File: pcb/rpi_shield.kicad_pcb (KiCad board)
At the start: 2 copper layers, 65 x 56 mm, 22 parts, among them IC1 ATTINY48-A, P1 CONN_02X20, P101 CONN_01X02, P102 CONN_01X02, P103 CONN_01X02, P104 CONN_01X02, Q1 AM4874N, Q2 AM4874N, Q3 AM4874N, U101 LM317AEMP

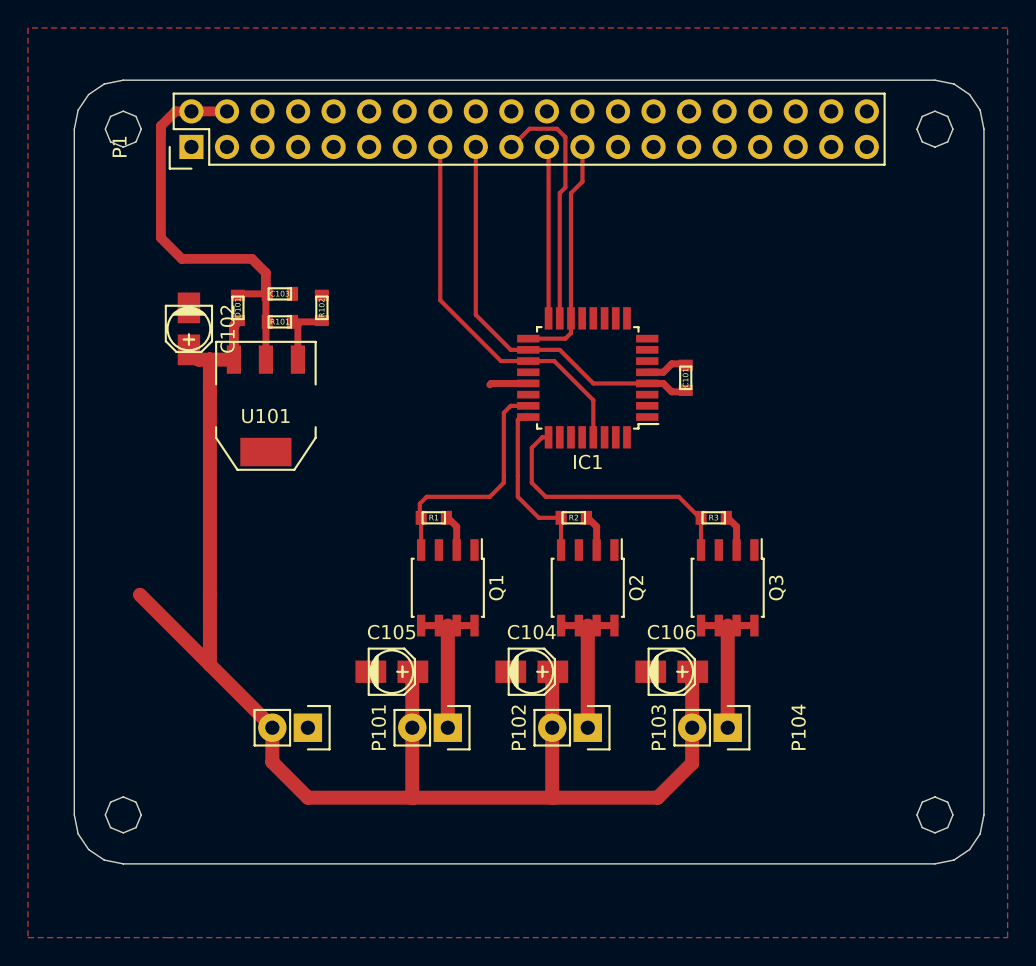
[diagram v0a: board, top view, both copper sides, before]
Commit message: swapped the mcu to a dac and a quad opamp
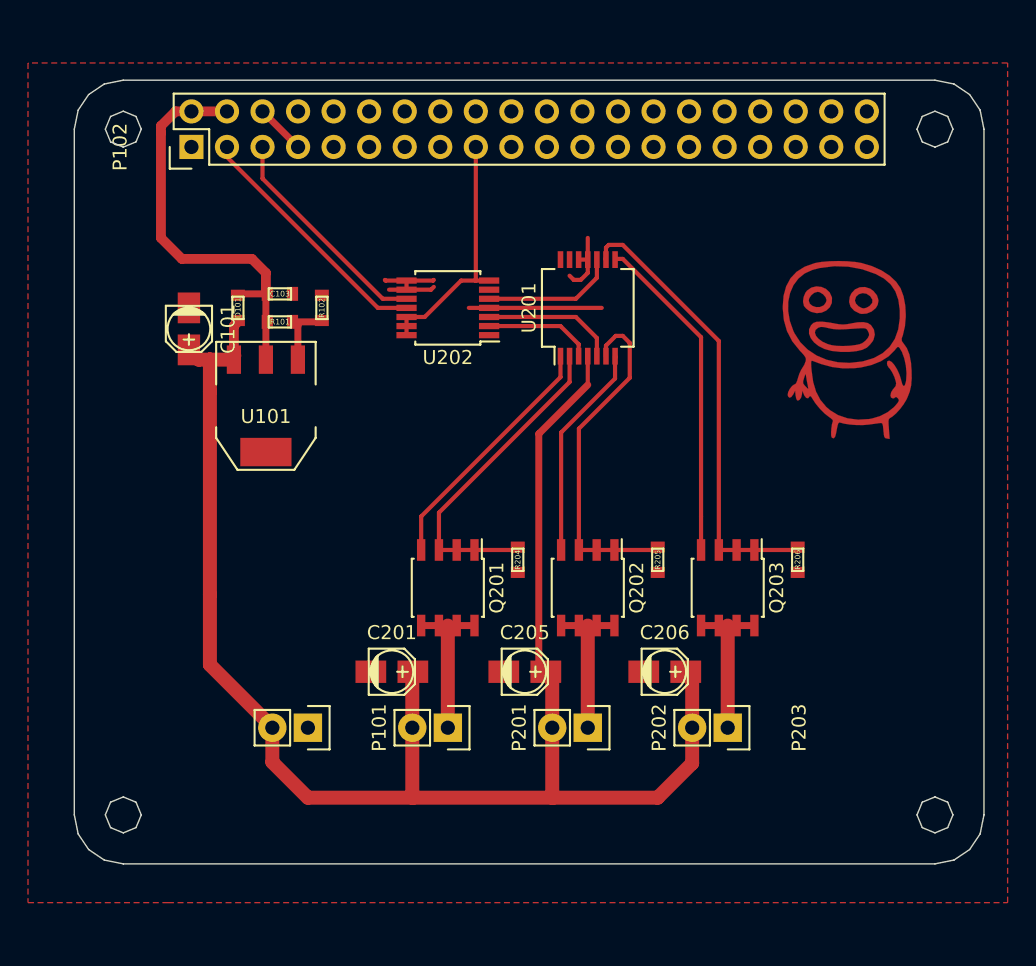
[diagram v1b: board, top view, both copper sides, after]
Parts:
- removed C102, C104, C105, C106: C, Capacitors_SMD:c_elec_3x5.3
- removed IC1: ATTINY48-A, Housings_QFP:TQFP-32_7x7mm_Pitch0.8mm
- removed P1: CONN_02X20, Pin_Headers:Pin_Header_Straight_2x20
- removed P103, P104: CONN_01X02, Pin_Headers:Pin_Header_Straight_1x02
- removed Q1, Q2, Q3: AM4874N, Housings_SOIC:SOIC-8_3.9x4.9mm_Pitch1.27mm
- removed R1, R2, R3: R, netl:SMD_0603
- added C201: C, Capacitors_SMD:c_elec_3x5.3, F.Cu at (121.0, 101.0)
- added C205: C, Capacitors_SMD:c_elec_3x5.3, F.Cu at (130.5, 101.0)
- added C206: C, Capacitors_SMD:c_elec_3x5.3, F.Cu at (140.5, 101.0)
- added G***: LOGO, netl:LOGO_127mm_copper, F.Cu at (153.5, 78.0)
- added P201: CONN_01X02, Pin_Headers:Pin_Header_Straight_1x02, F.Cu at (125.0, 105.0)
- added P202: CONN_01X02, Pin_Headers:Pin_Header_Straight_1x02, F.Cu at (135.0, 105.0)
- added P203: CONN_01X02, Pin_Headers:Pin_Header_Straight_1x02, F.Cu at (145.0, 105.0)
- added Q201: AM4874N, Housings_SOIC:SOIC-8_3.9x4.9mm_Pitch1.27mm, F.Cu at (125.0, 95.0)
- added Q202: AM4874N, Housings_SOIC:SOIC-8_3.9x4.9mm_Pitch1.27mm, F.Cu at (135.0, 95.0)
- added Q203: AM4874N, Housings_SOIC:SOIC-8_3.9x4.9mm_Pitch1.27mm, F.Cu at (145.0, 95.0)
- added R204: R, netl:SMD_0603, F.Cu at (130.0, 93.0)
- added R205: R, netl:SMD_0603, F.Cu at (140.0, 93.0)
- added R206: R, netl:SMD_0603, F.Cu at (150.0, 93.0)
- added U201: LM2902N, Housings_SSOP:SSOP-14_5.3x6.2mm_Pitch0.65mm, F.Cu at (135.0, 75.0)
- added U202: MAX5813, Housings_SSOP:TSSOP-14_4.4x5mm_Pitch0.65mm, F.Cu at (125.0, 75.0)
- C101: footprint netl:SMD_0603 -> Capacitors_SMD:c_elec_3x5.3
- P102: value CONN_01X02 -> CONN_02X20; footprint Pin_Headers:Pin_Header_Straight_1x02 -> Pin_Headers:Pin_Header_Straight_2x20
- moved P102 45.4 mm to (106.7, 63.5), turned to 90 degrees
- moved C101 35.7 mm to (106.5, 76.5), turned to 270 degrees
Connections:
- C101 pad 1: 3v3 -> Vdd
- P102 pad 1: /DrainRed -> 3v3
- P102 pad 2: Vdd -> 5V
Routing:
- net Net-(Q203-Pad1): track 0.00 -> 32.6 mm
- net RESET: track 27.5 -> 0.06 mm
- net Net-(Q202-Pad1): track 0.00 -> 25.0 mm
- net Net-(Q203-Pad4): track 0.00 -> 23.7 mm
- net Net-(Q201-Pad1): track 0.00 -> 23.6 mm
- net Net-(Q201-Pad4): track 0.00 -> 18.5 mm
- net SDA: track 0.00 -> 18.0 mm
- net Vdd: track 104.3 -> 122.1 mm
- net MOSI: track 17.8 -> 0.00 mm
- net SCK: track 16.9 -> 0.00 mm
- net SCL: track 0.00 -> 16.1 mm
- net Net-(Q202-Pad4): track 0.00 -> 15.5 mm
- net MISO: track 12.3 -> 0.34 mm
- net GND: track 13.5 -> 25.3 mm
- net /LED driver/DrainRed: track 0.00 -> 11.5 mm
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
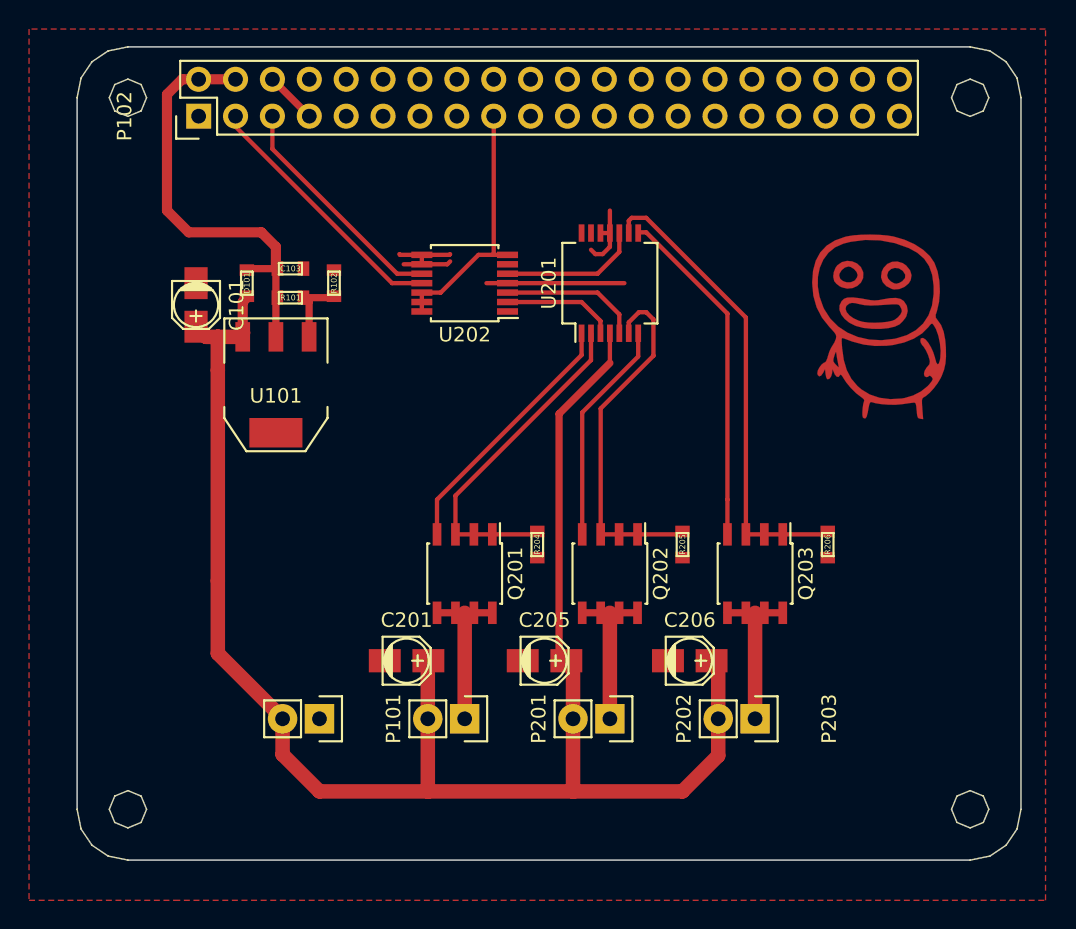
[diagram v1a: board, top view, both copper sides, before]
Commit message: removed excess power pins. moved parts around.
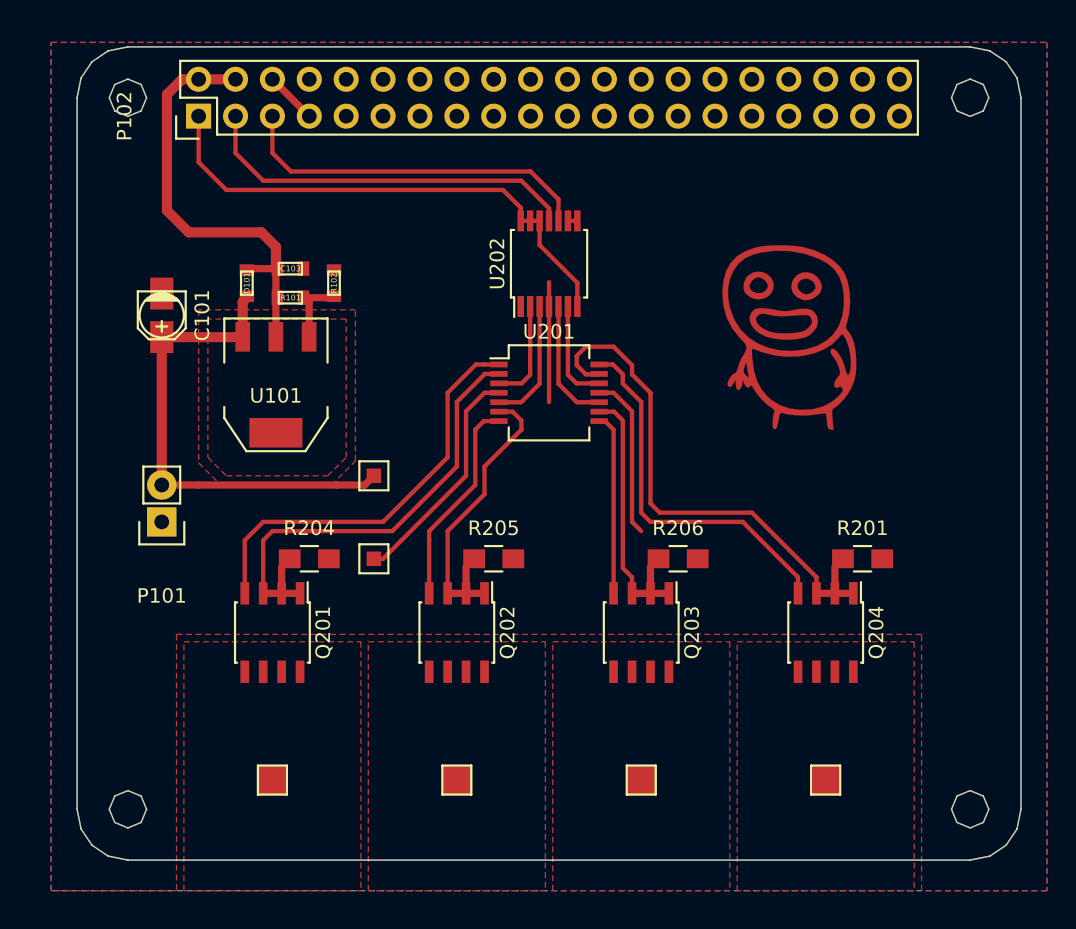
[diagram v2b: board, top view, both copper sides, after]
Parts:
- removed C201, C205, C206: C, Capacitors_SMD:c_elec_3x5.3
- added JP11: CONN_01X01, netl:1Pin_small, F.Cu at (118.7, 94.0)
- added JP11: CONN_01X01, netl:1Pin_small, F.Cu at (118.7, 88.3)
- added P204: CONN_01X01, netl:1Pin_big, F.Cu at (149.9, 109.2)
- added Q204: AM4874N, Housings_SOIC:SOIC-8_3.9x4.9mm_Pitch1.27mm, F.Cu at (149.9, 99.1)
- added R201: R, Resistors_SMD:R_0805_HandSoldering, F.Cu at (152.4, 94.0)
- P201, P202, P203: value CONN_01X02 -> CONN_01X01; footprint Pin_Headers:Pin_Header_Straight_1x02 -> netl:1Pin_big
- R204, R205, R206: footprint netl:SMD_0603 -> Resistors_SMD:R_0805_HandSoldering
- moved P101 17.4 mm to (104.1, 91.4), turned to 180 degrees
- moved R204 15.7 mm to (114.3, 94.0), turned to 0 degrees
- moved P201 13.9 mm to (111.8, 109.2)
- moved Q201 13.8 mm to (111.8, 99.1)
- moved R205 13.0 mm to (127.0, 94.0), turned to 0 degrees
- moved P202 11.4 mm to (124.5, 109.2)
- moved Q202 11.3 mm to (124.5, 99.1)
- moved R206 10.3 mm to (139.7, 94.0), turned to 0 degrees
- moved P203 8.90 mm to (137.2, 109.2)
- moved Q203 8.83 mm to (137.2, 99.1)
- moved U201 8.63 mm to (130.8, 82.5), turned to 0 degrees
- moved G*** 6.22 mm to (147.3, 78.7)
- moved U202 5.96 mm to (130.8, 73.7), turned to 90 degrees
- moved C101 2.47 mm to (104.1, 77.2)
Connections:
- U201 pad 12: GND -> W
- U202 pad 6: Net-(U202-Pad6) -> W
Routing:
- net Vdd: track 122.1 -> 49.4 mm
- net Net-(Q204-Pad1): track 0.00 -> 36.9 mm
- net Net-(Q204-Pad4): track 0.00 -> 25.7 mm
- net 3v3: track 17.9 -> 35.8 mm
- net Net-(Q203-Pad1): track 32.6 -> 18.9 mm
- net /LED driver/DrainRed: track 11.5 -> 0.00 mm
- net /LED driver/DrainGreen: track 11.5 -> 0.00 mm
- net /LED driver/DrainBlue: track 11.5 -> 0.00 mm
- net Net-(Q203-Pad4): track 23.7 -> 12.6 mm
- net Net-(Q201-Pad4): track 18.5 -> 28.8 mm
- net SDA: track 18.0 -> 27.3 mm
- net SCL: track 16.1 -> 25.0 mm
- net Net-(Q201-Pad1): track 23.6 -> 32.4 mm
- net W: track 0.00 -> 7.09 mm
- net Net-(Q202-Pad1): track 25.0 -> 21.0 mm
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- added copper zone on F.Cu, net /LED driver/DrainBlue
- added copper zone on F.Cu, net /LED driver/DrainGreen
- added copper zone on F.Cu, net /LED driver/DrainRed
- added copper zone on F.Cu, net /LED driver/DrainWhite
- added copper zone on F.Cu, net 5V
- added copper zone on B.Cu, net GND

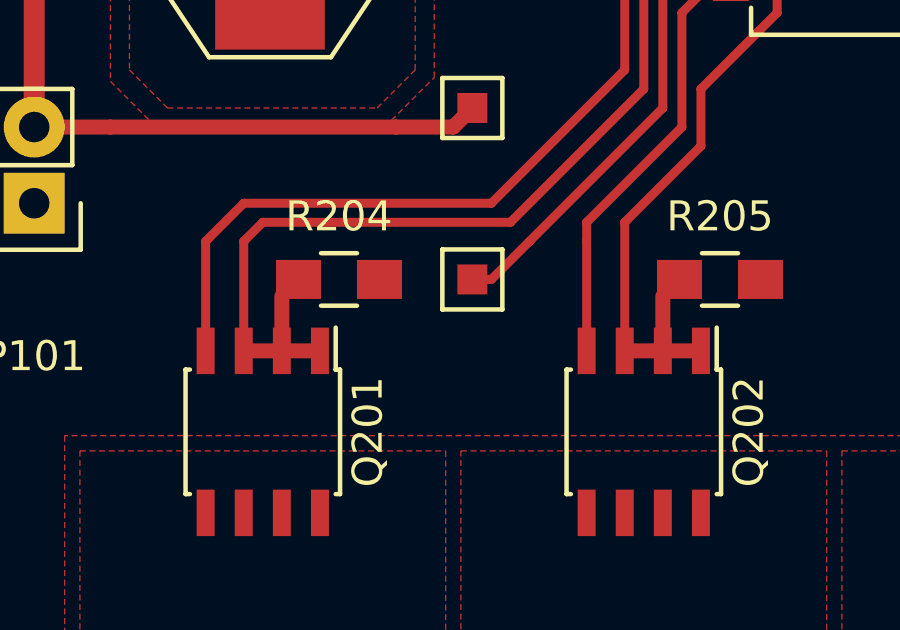
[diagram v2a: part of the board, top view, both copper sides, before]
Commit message: added cap for opamp
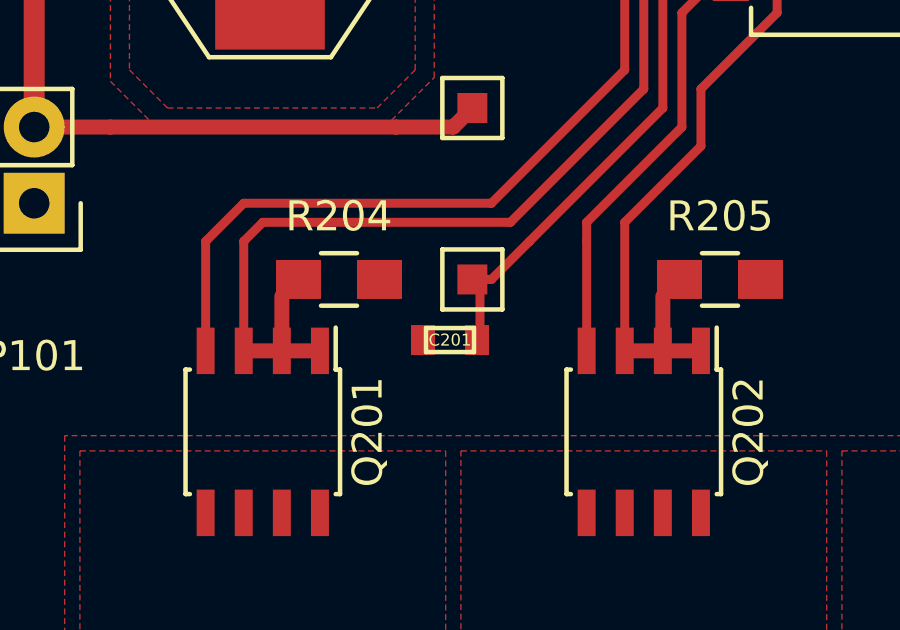
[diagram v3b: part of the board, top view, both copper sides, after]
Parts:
- added C201: C, netl:SMD_0603, F.Cu at (118.0, 96.0)
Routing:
- net Vdd: track 49.4 -> 51.5 mm
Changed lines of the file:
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@@
 (kicad_pcb (version 4) (host pcbnew 0.201509030901+6151~29~ubuntu14.04.1-product)
   (general
-    (links 78)
+    (links 80)
     (no_connects 2)
     (area 98.26011 58.679878 163.360114 114.779881)
     (thickness 1.6)
     (drawings 57)
-    (tracks 158)
+    (tracks 160)
     (zones 0)
-    (modules 25)
+    (modules 26)
     (nets 52)
   )
@@
   )
   (setup
-    (last_trace_width 0.5)
+    (last_trace_width 0.3)
     (user_trace_width 0.3)
     (user_trace_width 0.5)
@@
     (pad_to_mask_clearance 0.2)
     (aux_axis_origin 0 0)
+    (grid_origin 134 95.5)
     (visible_elements FFFFFF7F)
     (pcbplotparams
@@
       (net 12 Vdd))
   )
+  (module netl:SMD_0603 (layer F.Cu)
+    (at 118 96)
+    (fp_text reference C201 (at 0 0) (layer F.SilkS)
+      (effects (font (size 0.4 0.4) (thickness 0.05)))
+    )
+    (fp_text value C (at 0 -0.8) (layer F.Fab)
+      (effects (font (size 0.4 0.4) (thickness 0.1)))
+    )
+    (fp_line (start -0.8 0.4) (end 0.8 0.4) (layer F.SilkS) (width 0.15))
+    (fp_line (start 0.8 0.4) (end 0.8 -0.4) (layer F.SilkS) (width 0.15))
+    (fp_line (start 0.8 -0.4) (end -0.8 -0.4) (layer F.SilkS) (width 0.15))
+    (fp_line (start -0.8 -0.4) (end -0.8 0.4) (layer F.SilkS) (width 0.15))
+    (pad 1 smd rect (at -1 0) (size 0.8 1) (drill (offset 0.1 0)) (layers F.Cu F.Paste F.Mask)
+      (net 1 GND))
+    (pad 2 smd rect (at 1 0) (size 0.8 1) (drill (offset -0.1 0)) (layers F.Cu F.Paste F.Mask)
+      (net 12 Vdd))
+  )
   (gr_line (start 161.094491 62.229886) (end 161.094491 62.229886) (layer Dwgs.User) (width 0.1))
   (gr_line (start 160.718305 61.321695) (end 161.094491 62.229886) (layer Edge.Cuts) (width 0.1))
@@
   (segment (start 114.286 76.286) (end 114 76) (width 0.5) (layer F.Cu) (net 11))
   (segment (start 114 76) (end 116 76) (width 0.5) (layer F.Cu) (net 11) (status 20))
+  (segment (start 119 96) (end 119 94.235) (width 0.3) (layer F.Cu) (net 12))
+  (segment (start 119 94.235) (end 118.745 93.98) (width 0.3) (layer F.Cu) (net 12))
   (segment (start 118.745 88.265) (end 118.11 88.9) (width 0.5) (layer F.Cu) (net 12))
   (segment (start 116.205 88.9) (end 106.68 88.9) (width 0.5) (layer F.Cu) (net 12))
